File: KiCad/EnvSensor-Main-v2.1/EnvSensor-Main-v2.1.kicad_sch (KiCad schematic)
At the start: 87 parts, among them J6 POWER_INPUT, Q1 IRLML2502

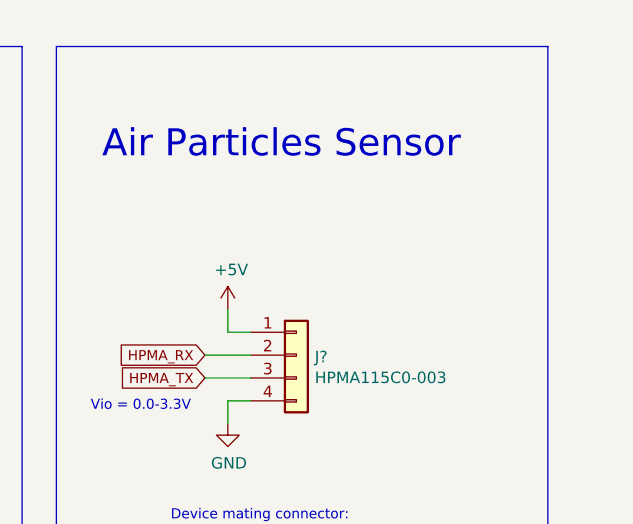
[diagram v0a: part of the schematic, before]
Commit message: hpma pinout
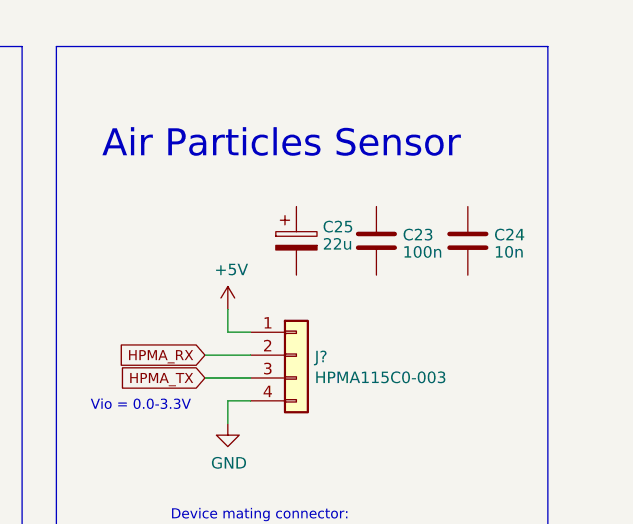
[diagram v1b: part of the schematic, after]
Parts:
- added C23: 100n, symbol Device:C
- added C24: 10n, symbol Device:C
- added C25: 22u, symbol Device:C_Polarized
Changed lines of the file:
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@@
+    )
+  )
+  (symbol (lib_id "Device:C") (at 386.08 44.45 0) (unit 1)
+    (in_bom yes) (on_board yes) (dnp no) (fields_autoplaced)
+    (property "Reference" "C23" (at 389.001 43.8063 0)
+      (effects (font (size 1.27 1.27)) (justify left))
+    )
+    (property "Value" "100n" (at 389.001 45.7273 0)
+      (effects (font (size 1.27 1.27)) (justify left))
+    )
+    (property "Footprint" "" (at 387.0452 48.26 0)
+      (effects (font (size 1.27 1.27)) hide)
+    )
+    (property "Datasheet" "~" (at 386.08 44.45 0)
+      (effects (font (size 1.27 1.27)) hide)
+    )
+    (pin "1")
+    (pin "2")
+    (instances
+      (project "EnvSensor-Main-v2.1"
+        (path "/dfd093c6-2284-47ad-b656-d7ad8b97da97"
+          (reference "C23") (unit 1)
+        )
+      )
     )
   )
@@
         (path "/dfd093c6-2284-47ad-b656-d7ad8b97da97"
           (reference "SW1") (unit 1)
+        )
+      )
+    )
+  )
+  (symbol (lib_id "Device:C") (at 396.24 44.45 0) (unit 1)
+    (in_bom yes) (on_board yes) (dnp no) (fields_autoplaced)
+    (property "Reference" "C24" (at 399.161 43.8063 0)
+      (effects (font (size 1.27 1.27)) (justify left))
+    )
+    (property "Value" "10n" (at 399.161 45.7273 0)
+      (effects (font (size 1.27 1.27)) (justify left))
+    )
+    (property "Footprint" "" (at 397.2052 48.26 0)
+      (effects (font (size 1.27 1.27)) hide)
+    )
+    (property "Datasheet" "~" (at 396.24 44.45 0)
+      (effects (font (size 1.27 1.27)) hide)
+    )
+    (pin "1")
+    (pin "2")
+    (instances
+      (project "EnvSensor-Main-v2.1"
+        (path "/dfd093c6-2284-47ad-b656-d7ad8b97da97"
+          (reference "C24") (unit 1)
         )
       )
@@
         )
       )
+    )
+  )
+  (symbol (lib_id "Device:C_Polarized") (at 377.19 44.45 0) (unit 1)
+    (in_bom yes) (on_board yes) (dnp no) (fields_autoplaced)
+    (property "Reference" "C25" (at 380.111 42.9173 0)
+      (effects (font (size 1.27 1.27)) (justify left))
+    )
+    (property "Value" "22u" (at 380.111 44.8383 0)
+      (effects (font (size 1.27 1.27)) (justify left))
+    )
+    (property "Footprint" "" (at 378.1552 48.26 0)
+      (effects (font (size 1.27 1.27)) hide)
+    )
+    (property "Datasheet" "~" (at 377.19 44.45 0)
+      (effects (font (size 1.27 1.27)) hide)
+    )
+    (pin "1")
+    (pin "2")
+    (instances
+      (project "EnvSensor-Main-v2.1"
+        (path "/dfd093c6-2284-47ad-b656-d7ad8b97da97"
+          (reference "C25") (unit 1)
+        )
+      )

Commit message: SOme fixes
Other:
- note added: "GPIO interrupts 1 e-Ink Busy 8 SCD30 Ready 12 Switch 1 13 Switch 2 14 Switch 3 15 Switch 4"
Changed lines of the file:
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@@
     (effects (font (size 1.1176 1.1176)) (justify left bottom))
+  )
+  (text "GPIO interrupts\n 1 e-Ink Busy\n 8 SCD30 Ready\n12 Switch 1\n13 Switch 2\n14 Switch 3\n15 Switch 4"
+    (at -69.85 223.52 0)
+    (effects (font (size 1.27 1.27)) (justify left bottom))
   )
   (text "Particles sensor is energised even when 5v power is off"

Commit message: Finishing
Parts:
- Y?: value 16Hz -> 16MHz
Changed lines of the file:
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@@
       (effects (font (size 1.27 1.27)) (justify left))
     )
-    (property "Value" "16Hz" (at 41.7576 114.173 90)
+    (property "Value" "16MHz" (at 41.7576 114.173 90)
       (effects (font (size 1.27 1.27)) (justify left))
     )

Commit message: Missing assignements fixed
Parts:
- C23: footprint (none) -> Capacitor_SMD:C_0603_1608Metric
- C24: footprint (none) -> Capacitor_SMD:C_0805_2012Metric
- C25: footprint (none) -> Capacitor_SMD:CP_Elec_6.3x5.8
- C45: footprint Capacitor_SMD:C_0805_2012Metric -> Capacitor_SMD:C_0603_1608Metric
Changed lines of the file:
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@@
       (effects (font (size 1.27 1.27)) (justify left))
     )
-    (property "Footprint" "Capacitor_SMD:C_0805_2012Metric" (at 357.8352 199.39 0)
+    (property "Footprint" "Capacitor_SMD:C_0603_1608Metric" (at 357.8352 199.39 0)
       (effects (font (size 1.27 1.27)) hide)
     )
@@
       (effects (font (size 1.27 1.27)) (justify left))
     )
-    (property "Footprint" "" (at 387.0452 48.26 0)
+    (property "Footprint" "Capacitor_SMD:C_0603_1608Metric" (at 387.0452 48.26 0)
       (effects (font (size 1.27 1.27)) hide)
     )
@@
       (effects (font (size 1.27 1.27)) (justify left))
     )
-    (property "Footprint" "" (at 397.2052 48.26 0)
+    (property "Footprint" "Capacitor_SMD:C_0805_2012Metric" (at 397.2052 48.26 0)
       (effects (font (size 1.27 1.27)) hide)
     )
@@
       (effects (font (size 1.27 1.27)) (justify left))
     )
-    (property "Footprint" "" (at 378.1552 48.26 0)
-      (effects (font (size 1.27 1.27)) hide)
-    )
+    (property "Footprint" "Capacitor_SMD:CP_Elec_6.3x5.8" (at 378.1552 48.26 0)
+      (effects (font (size 1.27 1.27)) hide)
+    )
